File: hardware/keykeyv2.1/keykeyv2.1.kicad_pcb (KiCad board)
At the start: 2 copper layers, 158.4 x 122.6 mm, 66 parts, among them J1 AudioJack4(PJ-320A), SW1 SW_Push, SW10 SW_Push, SW11 SW_Push, SW12 SW_Push, SW13 SW_Push, SW14 SW_Push, SW15 SW_Push, SW16 SW_Push, SW17 SW_Push, SW18 SW_Push, SW19 SW_Push, SW2 SW_Push, SW20 SW_Push, SW21 SW_Push, SW22 SW_Push, SW23 SW_Push, SW24 SW_Push, SW25 SW_Push, SW26 SW_Push, SW27 SW_Push, SW28 SW_Push, SW29 SW_Push, SW3 SW_Push, SW30 SW_Push, SW4 SW_Push, SW5 SW_Push, SW6 SW_Push, SW7 SW_Push, SW8 SW_Push, SW9 SW_Push, U2 5way-navigation-switch

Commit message: 업데이트
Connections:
- J1 pad 2: unconnected-(J1-Pad2) -> unconnected-(U1-GP26-Pad26)
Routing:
- net unconnected-(U1-GP26-Pad26): track 0.00 -> 36.8 mm, vias 0 -> 4
- net Net-(D13-K): track 143.0 -> 146.7 mm
- net Net-(U1-GP5): track 198.8 -> 201.1 mm
- net Net-(J1-Pad1): track 57.8 -> 59.9 mm
- net Net-(U1-GP3): track 198.2 -> 200.1 mm
- net Net-(U1-GP4): track 197.2 -> 199.0 mm
- net Net-(U1-GP2): track 218.2 -> 219.8 mm
- net Net-(U1-GP1): track 246.7 -> 248.0 mm

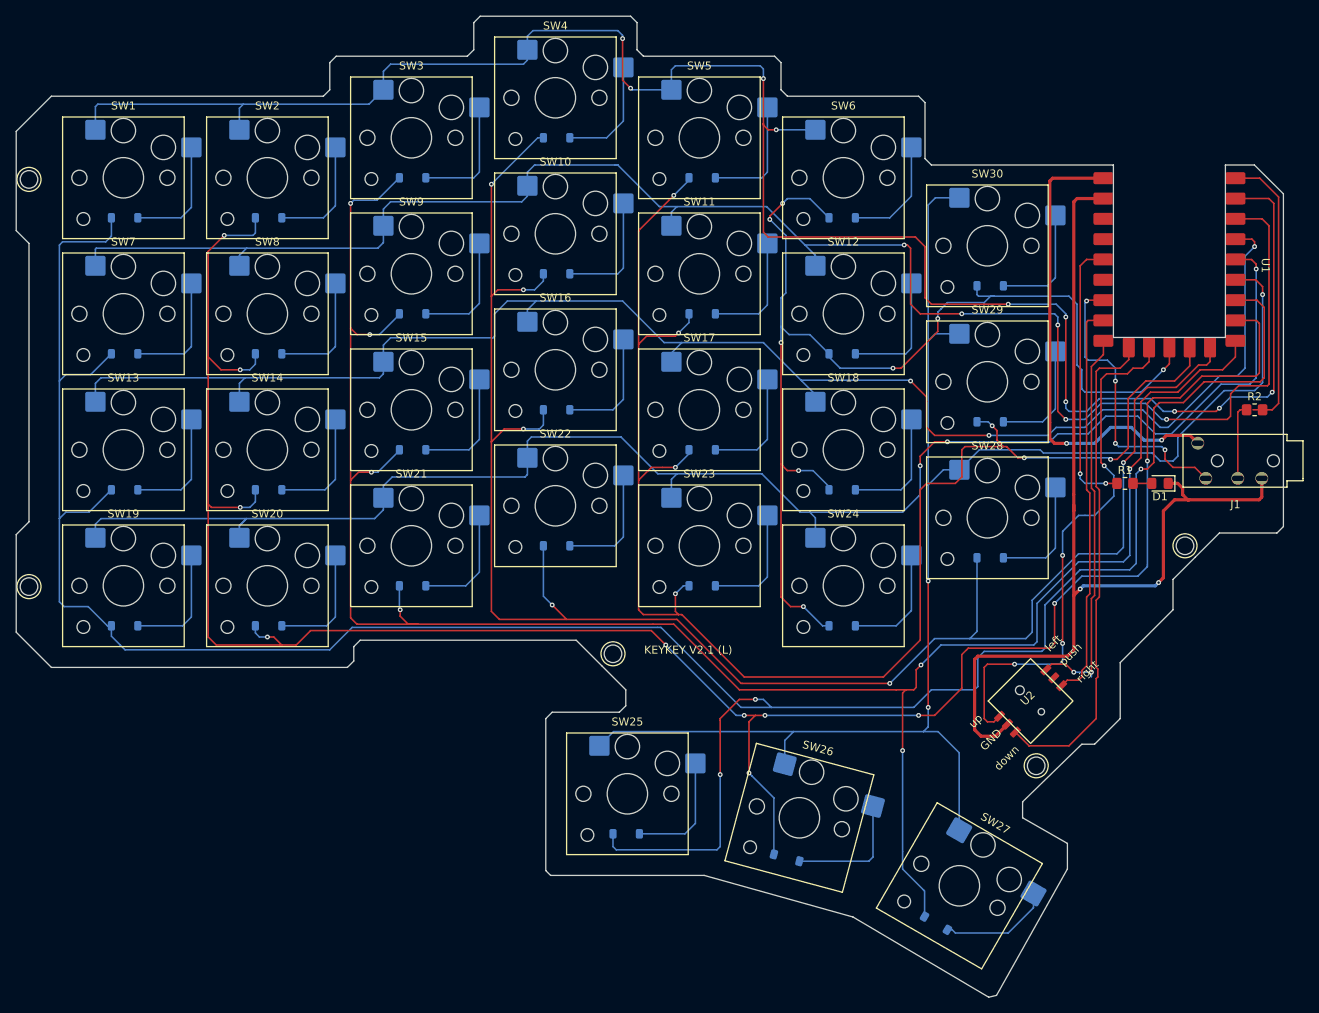
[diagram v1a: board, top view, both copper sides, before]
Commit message: kicad 파일 좌우 분리
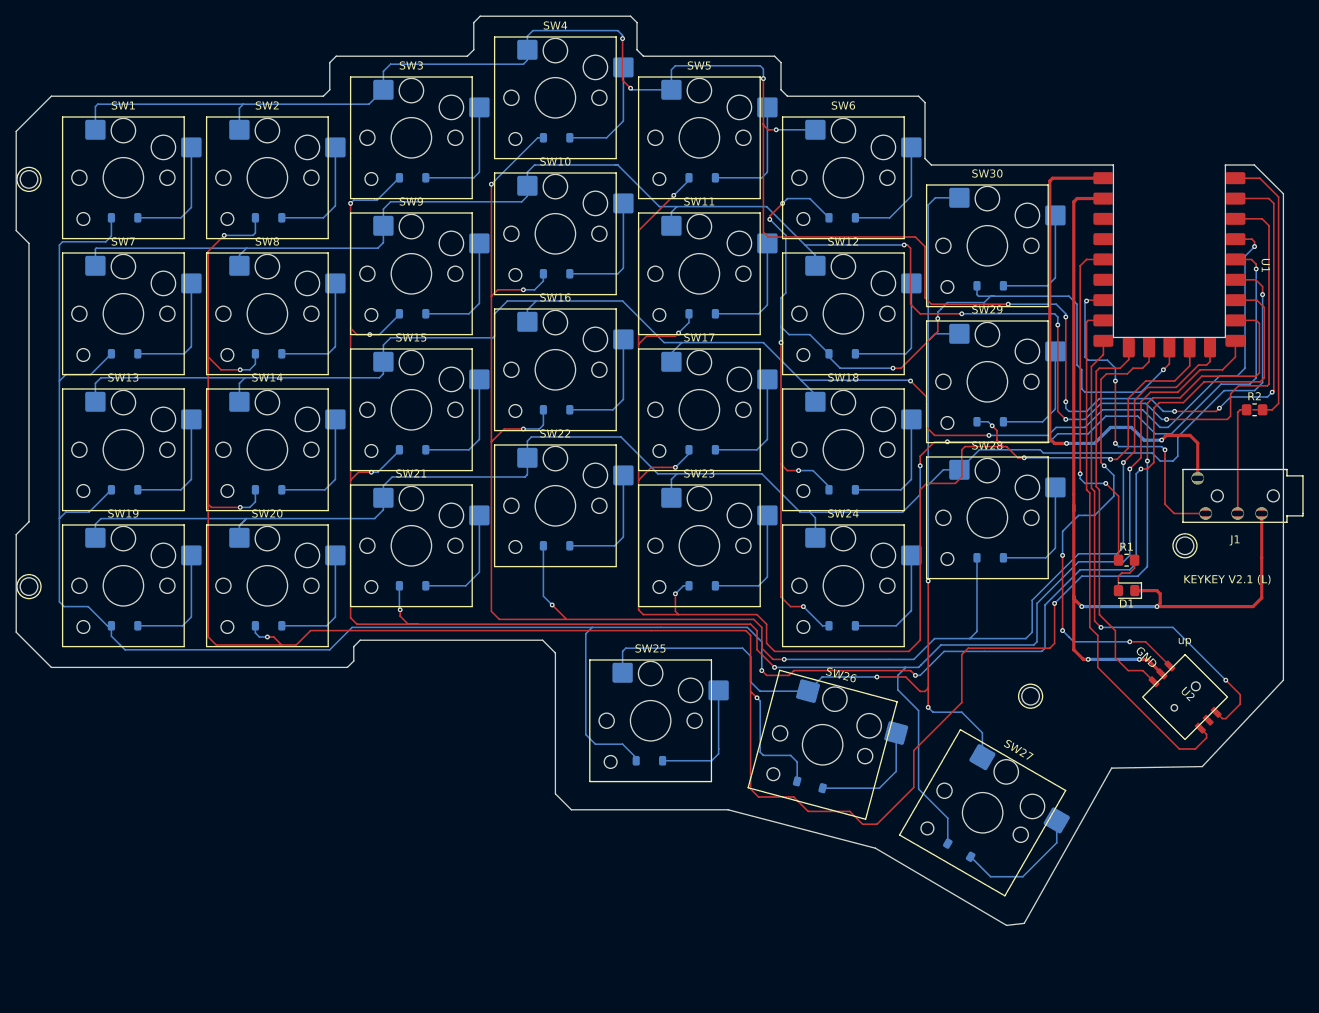
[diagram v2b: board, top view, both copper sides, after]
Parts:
- moved U2 19.3 mm to (132.7, 64.9), turned to -45 degrees
- moved D1 14.0 mm to (125.4, 51.6)
- moved R1 9.60 mm to (125.4, 47.8)
- moved D27 9.58 mm to (85.8, 75.9)
- moved SW25 9.58 mm to (65.9, 67.9)
- moved SW26 9.58 mm to (87.4, 70.9)
- moved SW27 9.58 mm to (107.4, 79.4)
- moved D26 9.58 mm to (65.8, 72.9)
- moved D28 9.58 mm to (104.5, 84.0)
- moved J1 4.39 mm to (147.4, 42.0)
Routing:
- net Net-(D15-K): track 278.1 -> 301.1 mm, vias 11 -> 7
- net Net-(D14-K): track 313.7 -> 293.4 mm
- net Net-(U1-GP15): track 50.1 -> 65.9 mm
- net Net-(D1-K): track 127.1 -> 113.0 mm, vias 2 -> 4
- net Net-(U1-GP14): track 49.4 -> 63.1 mm
- net Net-(U1-GP13): track 62.3 -> 49.1 mm
- net Net-(U1-GP28): track 34.7 -> 43.5 mm
- net Net-(U1-GP12): track 67.3 -> 59.8 mm
- net Net-(D10-K): track 258.7 -> 251.9 mm, vias 7 -> 6
- net Net-(U1-GP5): track 201.1 -> 194.7 mm, vias 3 -> 4
- net unconnected-(U1-GP26-Pad26): track 36.8 -> 41.9 mm
- net Net-(J1-Pad1): track 59.9 -> 64.3 mm
- net Net-(J1-Pad3): track 9.64 -> 13.9 mm
- net Net-(D1-A): track 2.56 -> 5.22 mm
- net Net-(D28-A): track 14.0 -> 16.4 mm
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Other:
- board size 158.4 x 122.6 mm -> 158.4 x 113.6 mm
